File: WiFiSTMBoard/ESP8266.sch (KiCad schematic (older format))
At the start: 2 parts

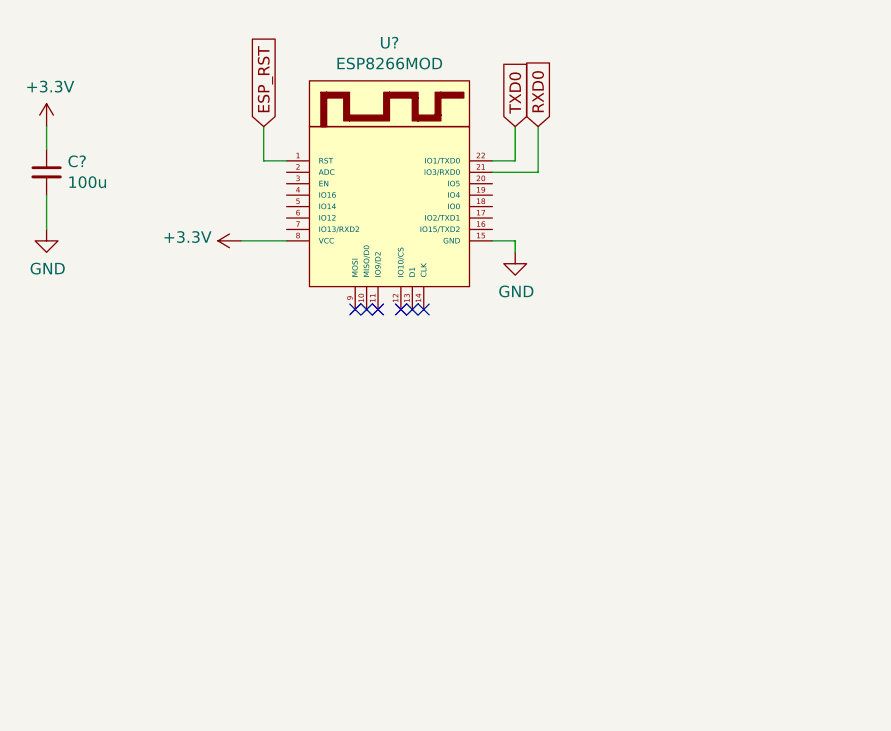
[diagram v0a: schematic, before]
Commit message: removed esp8266 diagram, added ch3040 diagram
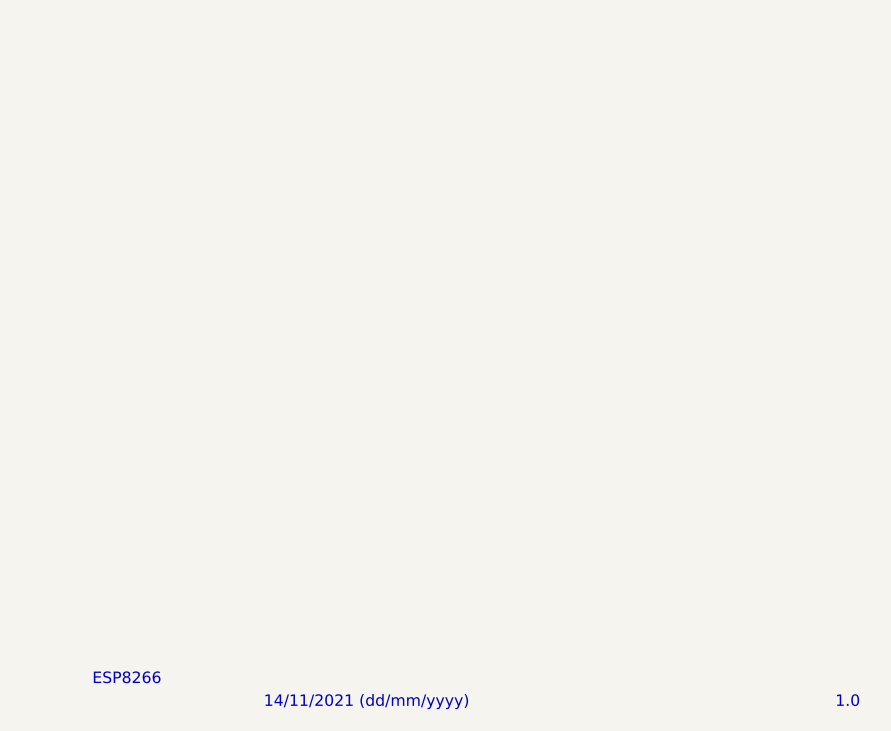
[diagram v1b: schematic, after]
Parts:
- removed C?: 100u, symbol Device:C_Small
- removed U?: ESP8266MOD, symbol RF_Module:ESP8266MOD
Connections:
- no-connect marks 6 -> 0
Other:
- note added: "1.0"
- note added: "14/11/2021 (dd/mm/yyyy)"
- note added: "ESP8266"
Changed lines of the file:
@@
 EELAYER 30 0
 EELAYER END
-$Descr A4 11693 8268
+$Descr User 8661 6299
 encoding utf-8
 Sheet 5 6
@@
 Comment4 ""
 $EndDescr
-$Comp
-L RF_Module:ESP8266MOD U?
-U 1 1 61986ACD
-P 5600 3450
-F 0 "U?" H 5600 4165 50  0000 C CNN
-F 1 "ESP8266MOD" H 5600 4074 50  0000 C CNN
-F 2 "" H 5600 4150 50  0001 C CNN
-F 3 "" H 5600 4150 50  0001 C CNN
-	1    5600 3450
-	1    0    0    -1
-$EndComp
-$Comp
-L power:GND #PWR?
-U 1 1 61987B7F
-P 6150 3650
-F 0 "#PWR?" H 6150 3400 50  0001 C CNN
-F 1 "GND" H 6155 3477 50  0000 C CNN
-F 2 "" H 6150 3650 50  0001 C CNN
-F 3 "" H 6150 3650 50  0001 C CNN
-	1    6150 3650
-	1    0    0    -1
-$EndComp
-Wire Wire Line
-	6050 3600 6150 3600
-Wire Wire Line
-	6150 3600 6150 3650
-$Comp
-L power:+3.3V #PWR?
-U 1 1 6198805F
-P 4950 3600
-F 0 "#PWR?" H 4950 3450 50  0001 C CNN
-F 1 "+3.3V" V 4965 3728 50  0000 L CNN
-F 2 "" H 4950 3600 50  0001 C CNN
-F 3 "" H 4950 3600 50  0001 C CNN
-	1    4950 3600
-	0    -1   -1   0
-$EndComp
-Wire Wire Line
-	4950 3600 5150 3600
-NoConn ~ 5450 3900
-NoConn ~ 5500 3900
-NoConn ~ 5550 3900
-NoConn ~ 5650 3900
-NoConn ~ 5700 3900
-NoConn ~ 5750 3900
-$Comp
-L Device:C_Small C?
-U 1 1 61989FF7
-P 4100 3300
-F 0 "C?" H 4192 3346 50  0000 L CNN
-F 1 "100u" H 4192 3255 50  0000 L CNN
-F 2 "" H 4100 3300 50  0001 C CNN
-F 3 "~" H 4100 3300 50  0001 C CNN
-	1    4100 3300
-	1    0    0    -1
-$EndComp
-$Comp
-L power:+3.3V #PWR?
-U 1 1 6198A395
-P 4100 3100
-F 0 "#PWR?" H 4100 2950 50  0001 C CNN
-F 1 "+3.3V" H 4115 3273 50  0000 C CNN
-F 2 "" H 4100 3100 50  0001 C CNN
-F 3 "" H 4100 3100 50  0001 C CNN
-	1    4100 3100
-	1    0    0    -1
-$EndComp
-$Comp
-L power:GND #PWR?
-U 1 1 6198AA9D
-P 4100 3550
-F 0 "#PWR?" H 4100 3300 50  0001 C CNN
-F 1 "GND" H 4105 3377 50  0000 C CNN
-F 2 "" H 4100 3550 50  0001 C CNN
-F 3 "" H 4100 3550 50  0001 C CNN
-	1    4100 3550
-	1    0    0    -1
-$EndComp
-Wire Wire Line
-	4100 3100 4100 3200
-Wire Wire Line
-	4100 3400 4100 3550
-Text GLabel 5050 3100 1    50   Input ~ 0
-ESP_RST
-Wire Wire Line
-	5150 3250 5050 3250
-Wire Wire Line
-	5050 3250 5050 3100
-Text GLabel 6150 3100 1    50   Input ~ 0
-TXD0
-Text GLabel 6250 3100 1    50   Input ~ 0
-RXD0
-Wire Wire Line
-	6050 3250 6150 3250
-Wire Wire Line
-	6150 3250 6150 3100
-Wire Wire Line
-	6050 3300 6250 3300
-Wire Wire Line
-	6250 3300 6250 3100
+Text Notes 4300 5550 0    50   ~ 0
+ESP8266
+Text Notes 5050 5650 0    50   ~ 0
+14/11/2021 (dd/mm/yyyy)
+Text Notes 7550 5650 0    50   ~ 0
+1.0
 $EndSCHEMATC
